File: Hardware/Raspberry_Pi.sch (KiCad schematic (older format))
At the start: 11 parts, among them J1 M20-9762042, J2 Motor_2, J3 Motor_1, J8 FTDI

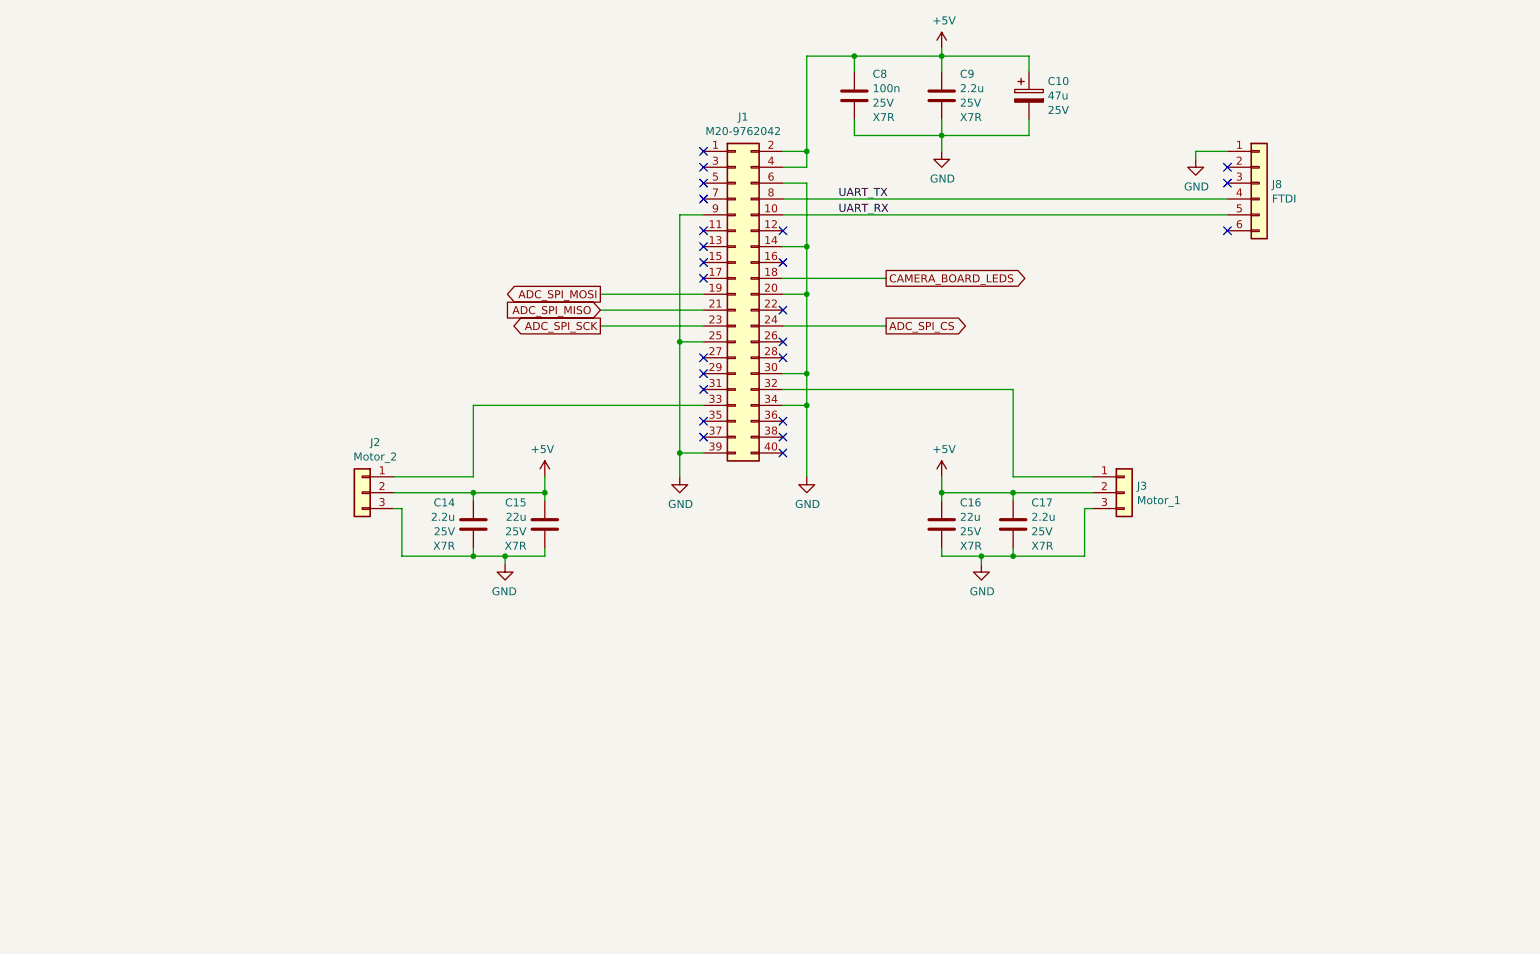
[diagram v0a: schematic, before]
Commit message: [Hardware] Added transistors to drive servomotors PWM signal with +5V instead of Raspberry Pi +3.3V.
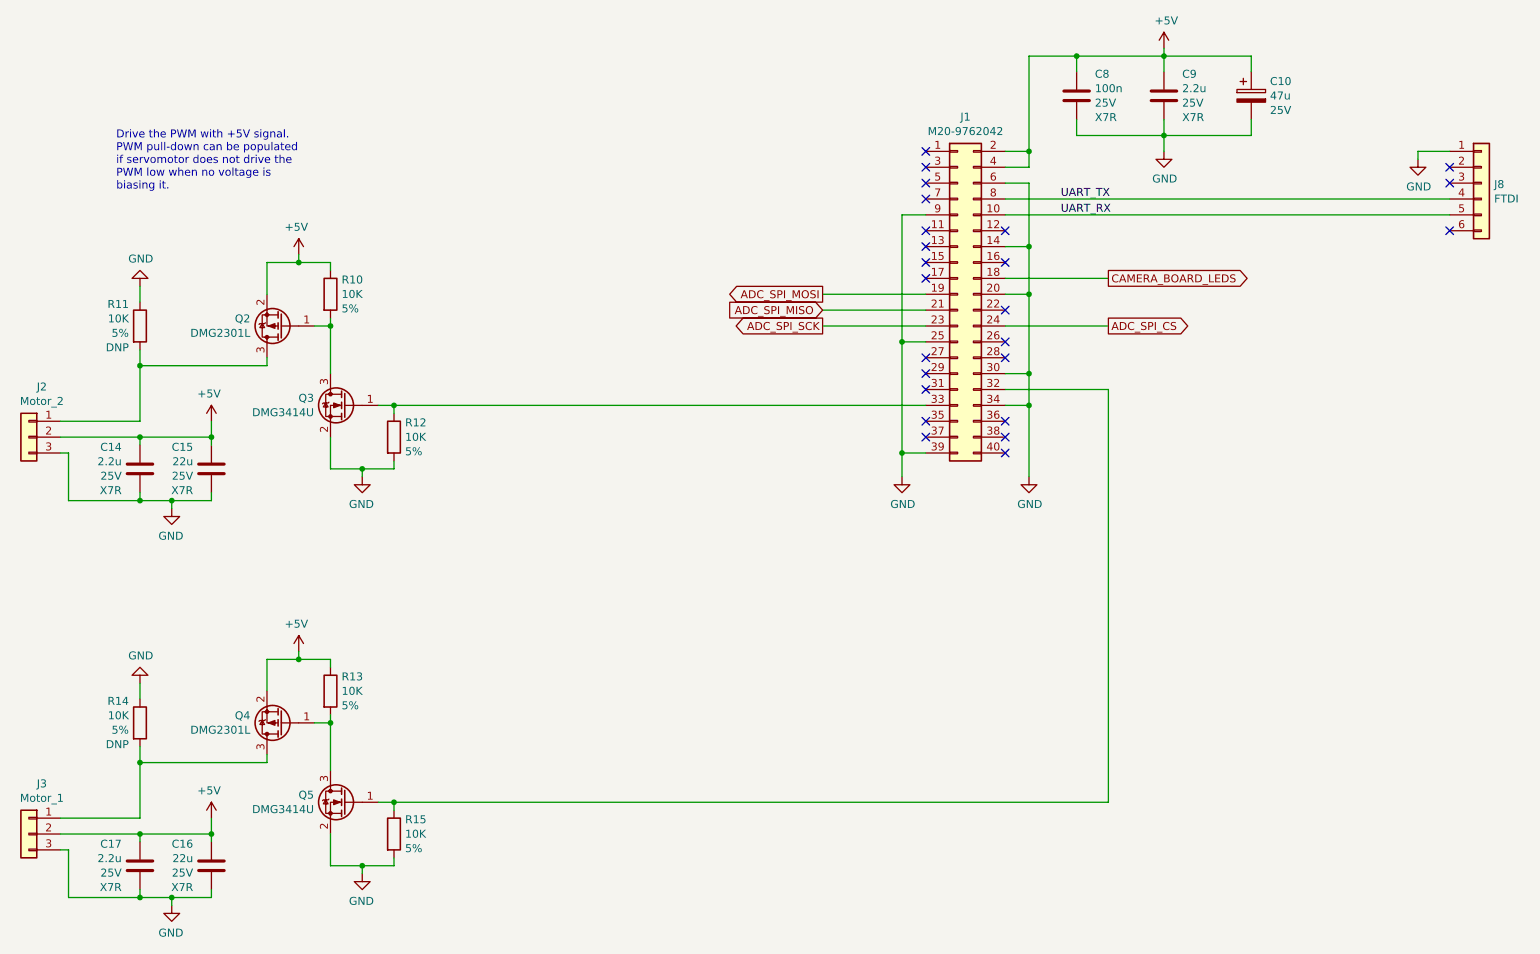
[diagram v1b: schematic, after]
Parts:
- added Q2, Q4: DMG2301L, Package_TO_SOT_SMD:SOT-23, symbol Transistor_FET:DMG2301L
- added Q3, Q5: DMG3414U, Package_TO_SOT_SMD:SOT-23, symbol Transistor_FET:DMG3414U
- added R10, R11, R12, R13, R14, R15: 10K, Resistor_SMD:R_1206_3216Metric_Pad1.42x1.75mm_HandSolder, symbol Device:R
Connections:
- net +5V: now also Q2.2 (S), Q4.2 (S), R10.1, R13.1
- net GND: now also Q3.2 (S), Q5.2 (S), R11.1, R12.2, R14.1, R15.2
- net at J3.1 (Pin_1): now also Q4.3 (D), R14.2; no longer J1.32 (Pin_32)
- net at J1.33 (Pin_33): now also Q3.1 (G), R12.1; no longer J2.1 (Pin_1)
- new net: Q2.1 (G), Q3.3 (D), R10.2
- new net: J1.32 (Pin_32), Q5.1 (G), R15.1
- new net: J2.1 (Pin_1), Q2.3 (D), R11.2
- new net: Q4.1 (G), Q5.3 (D), R13.2
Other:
- note added: "Drive the PWM with +5V signal.\nPWM pull-down can be populated\nif servomotor does not drive the\nPWM low when no voltage is\nbiasing it."
- moved on the sheet: C10, C14, C15, C16, C17, C8, C9, J1, J2, J3, J8

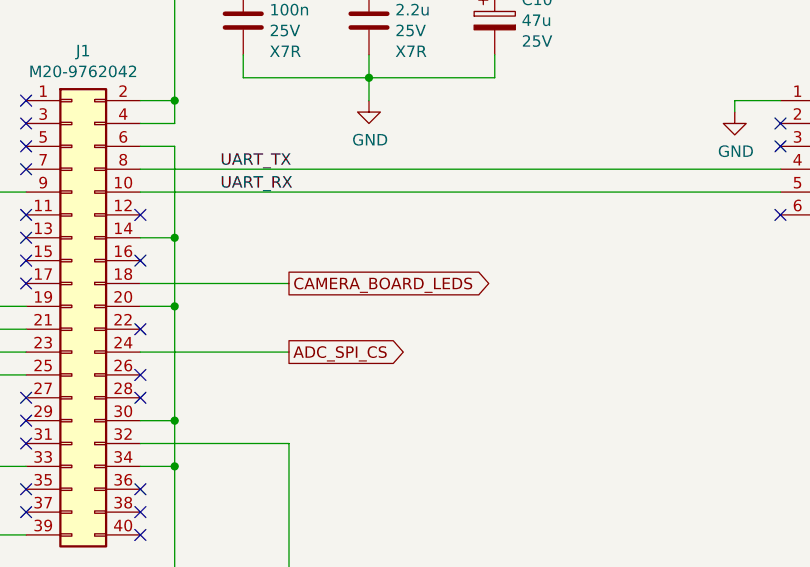
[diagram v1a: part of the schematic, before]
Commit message: [Hardware] Renamed 'camera board' to 'front board' as this board is not only carrying the camera.
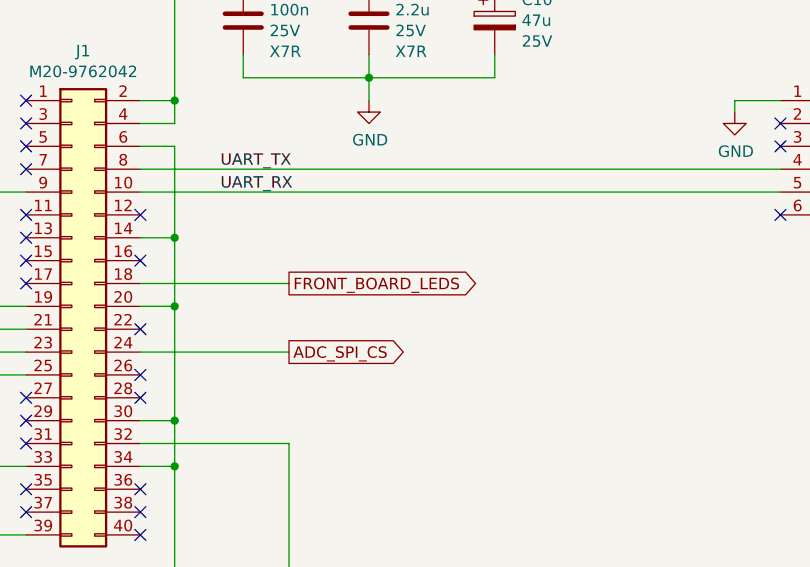
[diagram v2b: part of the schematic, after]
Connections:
- net CAMERA_BOARD_LEDS renamed FRONT_BOARD_LEDS
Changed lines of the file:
@@
 Connection ~ 2100 3850
 Text GLabel 7750 2850 2    50   Output ~ 0
-CAMERA_BOARD_LEDS
+FRONT_BOARD_LEDS
 NoConn ~ 6600 2050
 NoConn ~ 6600 2150

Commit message: [Hardware] Changed 22u capacitors footprint from 1206 to 1210 as more references are available in 1210 package.
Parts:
- C15, C16: footprint Capacitor_SMD:C_1206_3216Metric_Pad1.42x1.75mm_HandSolder -> Capacitor_SMD:C_1210_3225Metric_Pad1.42x2.65mm_HandSolder
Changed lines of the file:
@@
 F 0 "C16" H 1985 6413 50  0000 R CNN
 F 1 "22u" H 1985 6504 50  0000 R CNN
-F 2 "Capacitor_SMD:C_1206_3216Metric_Pad1.42x1.75mm_HandSolder" H 2138 6400 50  0001 C CNN
+F 2 "Capacitor_SMD:C_1210_3225Metric_Pad1.42x2.65mm_HandSolder" H 2138 6400 50  0001 C CNN
 F 3 "~" H 2100 6550 50  0001 C CNN
 F 4 "25V" H 1985 6595 50  0000 R CNN "Value2"
@@
 F 0 "C15" H 1985 3913 50  0000 R CNN
 F 1 "22u" H 1985 4004 50  0000 R CNN
-F 2 "Capacitor_SMD:C_1206_3216Metric_Pad1.42x1.75mm_HandSolder" H 2138 3900 50  0001 C CNN
+F 2 "Capacitor_SMD:C_1210_3225Metric_Pad1.42x2.65mm_HandSolder" H 2138 3900 50  0001 C CNN
 F 3 "~" H 2100 4050 50  0001 C CNN
 F 4 "25V" H 1985 4095 50  0000 R CNN "Value2"

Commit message: [Hardware] Changed R11 and R14 resistors value to 100ohm.
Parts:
- R11, R14: value 10K -> 100; Populate DNP -> (none)
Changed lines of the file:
@@
 AR Path="/5F1F2F9E/5F2D59D7" Ref="R?"  Part="1"
 AR Path="/5F22814A/5F2D59D7" Ref="R11"  Part="1"
-F 0 "R11" H 1580 3287 50  0000 R CNN
-F 1 "10K" H 1580 3196 50  0000 R CNN
+F 0 "R11" H 1720 3241 50  0000 L CNN
+F 1 "100" H 1720 3150 50  0000 L CNN
 F 2 "Resistor_SMD:R_1206_3216Metric_Pad1.42x1.75mm_HandSolder" V 1580 3150 50  0001 C CNN
 F 3 "~" H 1650 3150 50  0001 C CNN
-F 4 "5%" H 1580 3105 50  0000 R CNN "Value2"
-F 5 "DNP" H 1580 3014 50  0000 R CNN "Populate"
+F 4 "5%" H 1720 3059 50  0000 L CNN "Value2"
 	1    1650 3150
 	1    0    0    -1
@@
 AR Path="/5F1F2F9E/5F317798" Ref="R?"  Part="1"
 AR Path="/5F22814A/5F317798" Ref="R14"  Part="1"
-F 0 "R14" H 1580 5787 50  0000 R CNN
-F 1 "10K" H 1580 5696 50  0000 R CNN
+F 0 "R14" H 1720 5741 50  0000 L CNN
+F 1 "100" H 1720 5650 50  0000 L CNN
 F 2 "Resistor_SMD:R_1206_3216Metric_Pad1.42x1.75mm_HandSolder" V 1580 5650 50  0001 C CNN
 F 3 "~" H 1650 5650 50  0001 C CNN
-F 4 "5%" H 1580 5605 50  0000 R CNN "Value2"
-F 5 "DNP" H 1580 5514 50  0000 R CNN "Populate"
+F 4 "5%" H 1720 5559 50  0000 L CNN "Value2"
 	1    1650 5650
 	1    0    0    -1
